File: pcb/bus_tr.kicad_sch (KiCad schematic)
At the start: 9 parts, among them U19 74LS245, U20 74LS245, U5 74LS245, U6 74LS245, U7 74LS245, U8 74LS245

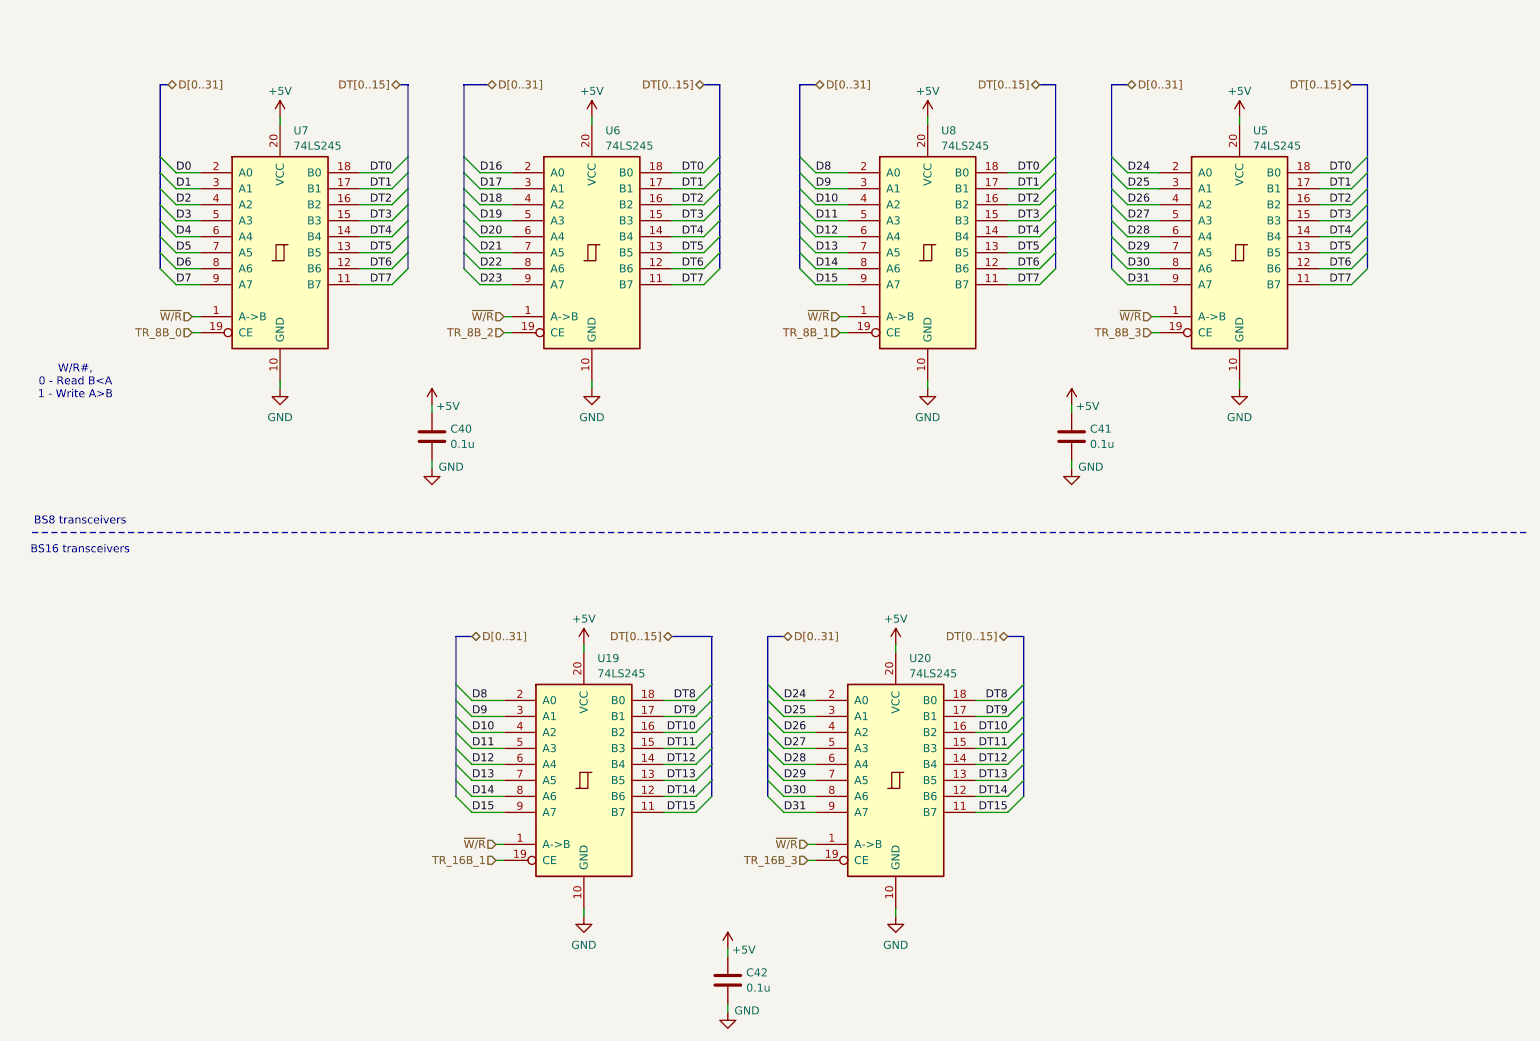
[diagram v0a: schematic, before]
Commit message: avr bus_tr diagrams aligned to grid
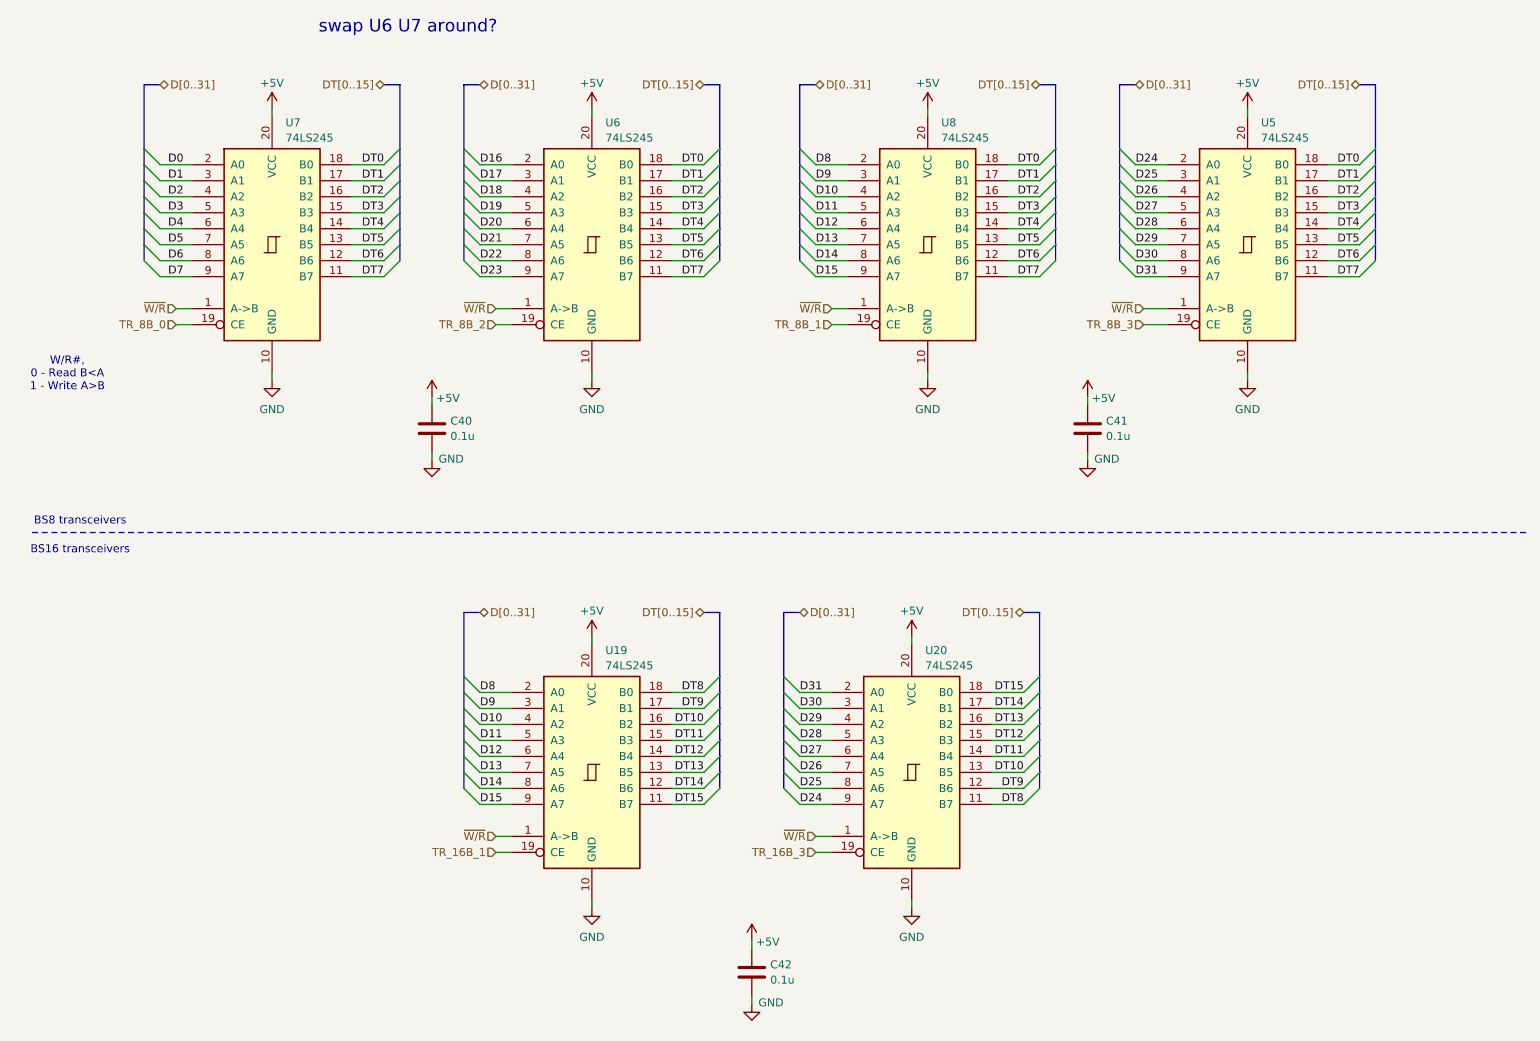
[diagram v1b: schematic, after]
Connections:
- net D24: now also U20.9 (A7); no longer U20.2 (A0)
- net D25: now also U20.8 (A6); no longer U20.3 (A1)
- net D26: now also U20.7 (A5); no longer U20.4 (A2)
- net D27: now also U20.6 (A4); no longer U20.5 (A3)
- net D28: now also U20.5 (A3); no longer U20.6 (A4)
- net D29: now also U20.4 (A2); no longer U20.7 (A5)
- net D30: now also U20.3 (A1); no longer U20.8 (A6)
- net D31: now also U20.2 (A0); no longer U20.9 (A7)
- net DT10: now also U20.13 (B5); no longer U20.16 (B2)
- net DT11: now also U20.14 (B4); no longer U20.15 (B3)
- net DT12: now also U20.15 (B3); no longer U20.14 (B4)
- net DT13: now also U20.16 (B2); no longer U20.13 (B5)
- net DT14: now also U20.17 (B1); no longer U20.12 (B6)
- net DT15: now also U20.18 (B0); no longer U20.11 (B7)
- net DT8: now also U20.11 (B7); no longer U20.18 (B0)
- net DT9: now also U20.12 (B6); no longer U20.17 (B1)
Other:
- note added: "swap U6 U7 around?"
- moved on the sheet: C40, C41, C42, U19, U20, U5, U6, U7, U8

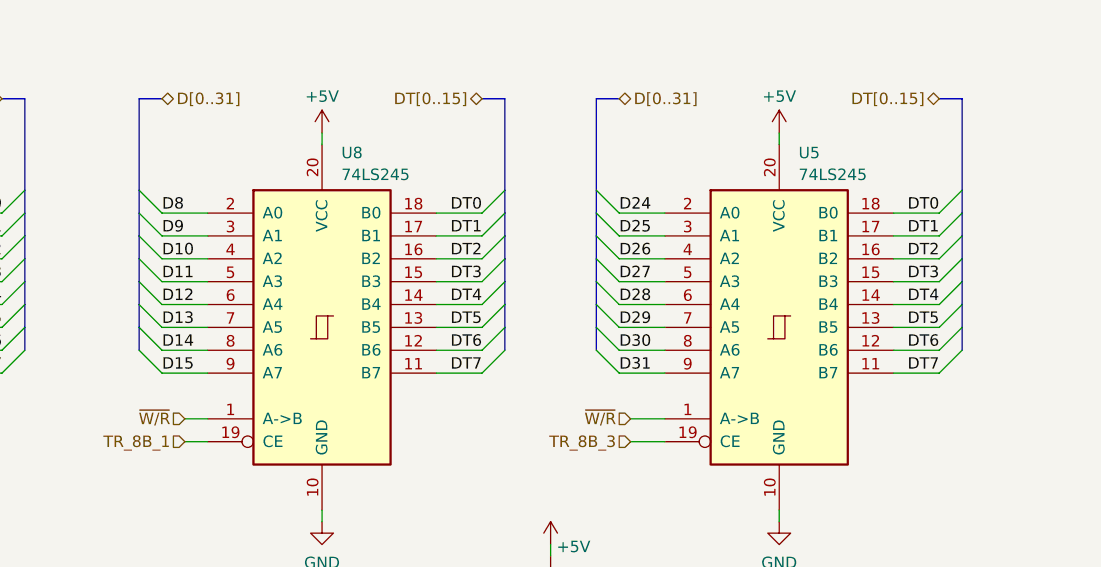
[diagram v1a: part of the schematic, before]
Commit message: reshuffled data order in upper word of data transceivers U5 U8 for easier layout
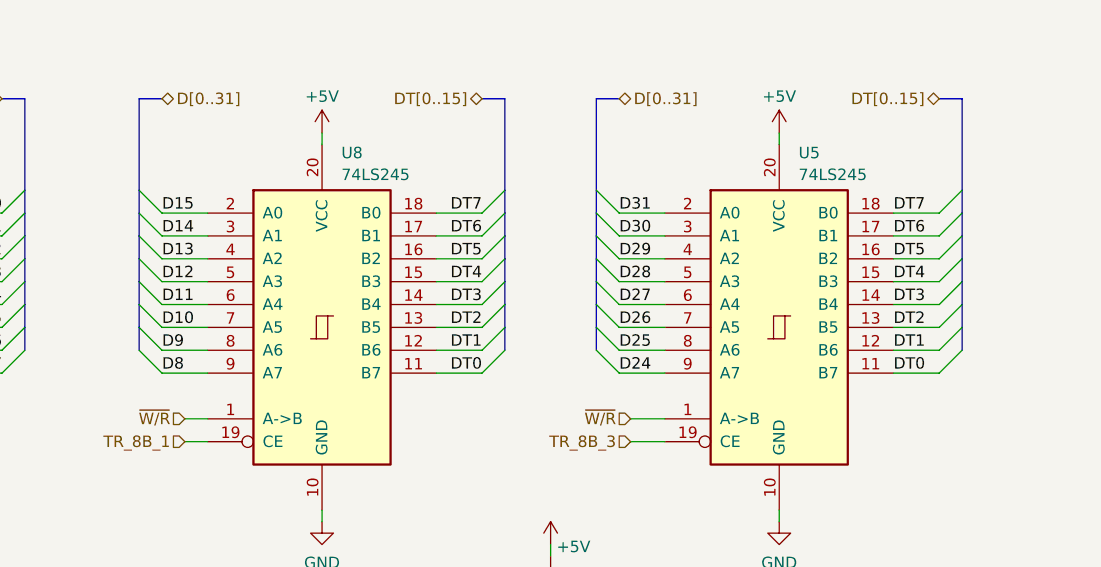
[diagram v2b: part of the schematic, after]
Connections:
- net D10: now also U8.7 (A5); no longer U8.4 (A2)
- net D11: now also U8.6 (A4); no longer U8.5 (A3)
- net D12: now also U8.5 (A3); no longer U8.6 (A4)
- net D13: now also U8.4 (A2); no longer U8.7 (A5)
- net D14: now also U8.3 (A1); no longer U8.8 (A6)
- net D15: now also U8.2 (A0); no longer U8.9 (A7)
- net D24: now also U5.9 (A7); no longer U5.2 (A0)
- net D25: now also U5.8 (A6); no longer U5.3 (A1)
- net D26: now also U5.7 (A5); no longer U5.4 (A2)
- net D27: now also U5.6 (A4); no longer U5.5 (A3)
- net D28: now also U5.5 (A3); no longer U5.6 (A4)
- net D29: now also U5.4 (A2); no longer U5.7 (A5)
- net D30: now also U5.3 (A1); no longer U5.8 (A6)
- net D31: now also U5.2 (A0); no longer U5.9 (A7)
- net D8: now also U8.9 (A7); no longer U8.2 (A0)
- net D9: now also U8.8 (A6); no longer U8.3 (A1)
- net DT0: now also U5.11 (B7), U8.11 (B7); no longer U5.18 (B0), U8.18 (B0)
- net DT1: now also U5.12 (B6), U8.12 (B6); no longer U5.17 (B1), U8.17 (B1)
- net DT2: now also U5.13 (B5), U8.13 (B5); no longer U5.16 (B2), U8.16 (B2)
- net DT3: now also U5.14 (B4), U8.14 (B4); no longer U5.15 (B3), U8.15 (B3)
- net DT4: now also U5.15 (B3), U8.15 (B3); no longer U5.14 (B4), U8.14 (B4)
- net DT5: now also U5.16 (B2), U8.16 (B2); no longer U5.13 (B5), U8.13 (B5)
- net DT6: now also U5.17 (B1), U8.17 (B1); no longer U5.12 (B6), U8.12 (B6)
- net DT7: now also U5.18 (B0), U8.18 (B0); no longer U5.11 (B7), U8.11 (B7)
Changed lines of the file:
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@@
 	(wire
 		(pts
-			(xy 231.14 40.64) (xy 236.22 40.64)
+			(xy 236.22 58.42) (xy 231.14 58.42)
 		)
 		(stroke
@@
 	(wire
 		(pts
-			(xy 231.14 58.42) (xy 236.22 58.42)
+			(xy 236.22 40.64) (xy 231.14 40.64)
 		)
 		(stroke
@@
 	(wire
 		(pts
-			(xy 231.14 50.8) (xy 236.22 50.8)
+			(xy 236.22 48.26) (xy 231.14 48.26)
 		)
 		(stroke
@@
 	(wire
 		(pts
-			(xy 205.74 40.64) (xy 200.66 40.64)
+			(xy 200.66 40.64) (xy 205.74 40.64)
 		)
 		(stroke
@@
 	(wire
 		(pts
-			(xy 231.14 55.88) (xy 236.22 55.88)
+			(xy 236.22 43.18) (xy 231.14 43.18)
 		)
 		(stroke
@@
 	(wire
 		(pts
-			(xy 231.14 48.26) (xy 236.22 48.26)
+			(xy 236.22 50.8) (xy 231.14 50.8)
 		)
 		(stroke
@@
 	(wire
 		(pts
-			(xy 231.14 53.34) (xy 236.22 53.34)
+			(xy 236.22 45.72) (xy 231.14 45.72)
 		)
 		(stroke
@@
 	(wire
 		(pts
-			(xy 231.14 45.72) (xy 236.22 45.72)
+			(xy 236.22 53.34) (xy 231.14 53.34)
 		)
 		(stroke
@@
 	(wire
 		(pts
-			(xy 231.14 43.18) (xy 236.22 43.18)
+			(xy 236.22 55.88) (xy 231.14 55.88)
 		)
 		(stroke
@@
 	)
 	(label "DT3"
-		(at 236.22 48.26 180)
-		(effects
-			(font
-				(size 1.27 1.27)
-			)
-			(justify right bottom)
+		(at 231.14 50.8 0)
+		(effects
+			(font
+				(size 1.27 1.27)
+			)
+			(justify left bottom)
 		)
 	)
@@
 	)
 	(label "DT0"
-		(at 236.22 40.64 180)
-		(effects
-			(font
-				(size 1.27 1.27)
-			)
-			(justify right bottom)
+		(at 231.14 58.42 0)
+		(effects
+			(font
+				(size 1.27 1.27)
+			)
+			(justify left bottom)
 		)
 	)
 	(label "DT1"
-		(at 185.42 43.18 180)
+		(at 185.42 55.88 180)
 		(effects
 			(font
@@
 	)
 	(label "DT7"
-		(at 185.42 58.42 180)
+		(at 185.42 40.64 180)
 		(effects
 			(font
@@
 	)
 	(label "D27"
-		(at 200.66 48.26 0)
+		(at 200.66 50.8 0)
 		(effects
 			(font
@@
 	)
 	(label "DT4"
-		(at 185.42 50.8 180)
+		(at 185.42 48.26 180)
 		(effects
 			(font
@@
 	)
 	(label "D15"
-		(at 149.86 58.42 0)
+		(at 149.86 40.64 0)
 		(effects
 			(font
@@
 	)
 	(label "D28"
-		(at 200.66 50.8 0)
+		(at 200.66 48.26 0)
 		(effects
 			(font
@@
 	)
 	(label "D13"
-		(at 149.86 53.34 0)
+		(at 149.86 45.72 0)
 		(effects
 			(font
@@
 	)
 	(label "D8"
-		(at 149.86 40.64 0)
+		(at 149.86 58.42 0)
 		(effects
 			(font
@@
 	)
 	(label "D30"
-		(at 200.66 55.88 0)
+		(at 200.66 43.18 0)
 		(effects
 			(font
@@
 	)
 	(label "D11"
-		(at 149.86 48.26 0)
+		(at 149.86 50.8 0)
 		(effects
 			(font
@@
 	)
 	(label "D24"
-		(at 200.66 40.64 0)
+		(at 200.66 58.42 0)
 		(effects
 			(font
@@
 	)
 	(label "DT2"
-		(at 236.22 45.72 180)
-		(effects
-			(font
-				(size 1.27 1.27)
-			)
-			(justify right bottom)
+		(at 231.14 53.34 0)
+		(effects
+			(font
+				(size 1.27 1.27)
+			)
+			(justify left bottom)
 		)
 	)
@@
 	)
 	(label "D9"
-		(at 149.86 43.18 0)
+		(at 149.86 55.88 0)
 		(effects
 			(font
@@
 	)
 	(label "DT5"
-		(at 185.42 53.34 180)
+		(at 185.42 45.72 180)
 		(effects
 			(font
@@
 	)
 	(label "D14"
-		(at 149.86 55.88 0)
+		(at 149.86 43.18 0)
 		(effects
 			(font
@@
 	)
 	(label "DT4"
-		(at 236.22 50.8 180)
-		(effects
-			(font
-				(size 1.27 1.27)
-			)
-			(justify right bottom)
+		(at 231.14 48.26 0)
+		(effects
+			(font
+				(size 1.27 1.27)
+			)
+			(justify left bottom)
 		)
 	)
@@
 	)
 	(label "DT5"
-		(at 236.22 53.34 180)
-		(effects
-			(font
-				(size 1.27 1.27)
-			)
-			(justify right bottom)
+		(at 231.14 45.72 0)
+		(effects
+			(font
+				(size 1.27 1.27)
+			)
+			(justify left bottom)
 		)
 	)
@@
 	)
 	(label "D25"
-		(at 200.66 43.18 0)
+		(at 200.66 55.88 0)
 		(effects
 			(font
@@
 	)
 	(label "DT3"
-		(at 185.42 48.26 180)
+		(at 185.42 50.8 180)
 		(effects
 			(font
@@
 	)
 	(label "D10"
-		(at 149.86 45.72 0)
+		(at 149.86 53.34 0)
 		(effects
 			(font
@@
 	)
 	(label "DT1"
-		(at 236.22 43.18 180)
-		(effects
-			(font
-				(size 1.27 1.27)
-			)
-			(justify right bottom)
+		(at 231.14 55.88 0)
+		(effects
+			(font
+				(size 1.27 1.27)
+			)
+			(justify left bottom)
 		)
 	)
@@
 	)
 	(label "DT6"
-		(at 185.42 55.88 180)
+		(at 185.42 43.18 180)
 		(effects
 			(font
@@
 	)
 	(label "D31"
-		(at 200.66 58.42 0)
+		(at 200.66 40.64 0)
 		(effects
 			(font
@@
 	)
 	(label "DT6"
-		(at 236.22 55.88 180)
-		(effects
-			(font
-				(size 1.27 1.27)
-			)
-			(justify right bottom)
+		(at 231.14 43.18 0)
+		(effects
+			(font
+				(size 1.27 1.27)
+			)
+			(justify left bottom)
 		)
 	)
@@
 	)
 	(label "DT0"
-		(at 185.42 40.64 180)
+		(at 185.42 58.42 180)
 		(effects
 			(font
@@
 	)
 	(label "D26"
-		(at 200.66 45.72 0)
+		(at 200.66 53.34 0)
 		(effects
 			(font
@@
 	)
 	(label "DT7"
-		(at 236.22 58.42 180)
-		(effects
-			(font
-				(size 1.27 1.27)
-			)
-			(justify right bottom)
+		(at 231.14 40.64 0)
+		(effects
+			(font
+				(size 1.27 1.27)
+			)
+			(justify left bottom)
 		)
 	)
@@
 	)
 	(label "D12"
-		(at 149.86 50.8 0)
+		(at 149.86 48.26 0)
 		(effects
 			(font
@@
 	)
 	(label "D29"
-		(at 200.66 53.34 0)
+		(at 200.66 45.72 0)
 		(effects
 			(font
@@
 	)
 	(label "DT2"
-		(at 185.42 45.72 180)
-		(effects
-			(font
+		(at 185.42 53.34 180)
+		(effects
+			(font
